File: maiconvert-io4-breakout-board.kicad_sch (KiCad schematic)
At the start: 86 parts, among them J1 CN3 - From IO4, J10 1P B7, J11 1P B8, J12 2P B1, J13 2P B2, J14 2P B3, J15 2P B4, J16 2P B5, J17 2P B6, J18 2P B7, J19 2P B8, J2 CN9 - From IO4, J20 1P SELECT BUTTON, J21 2P SELECT BUTTON, J22 12V input, J23 BILLBOARD LED L, J24 BILLBOARD LED R, J25 1P CODE READER LED, J26 2P CODE READER LED, J27 COIN METER, J28 COIN LOCKOUT, J29 CAMERA LED RED, J3 CN3 - To Harness, J30 CAMERA LED WARM, J31 TEST BUTTON, J32 COIN BUTTON, J33 SERVICE BUTTON, J4 1P B1, J5 1P B2, J6 1P B3, J7 1P B4, J8 1P B5, J9 1P B6, SW1 TEST, SW10 1P B5 BTN, SW11 1P B6 BTN, SW12 1P B7 BTN, SW13 1P B8 BTN, SW14 2P B1 BTN, SW15 2P B2 BTN, SW16 2P B3 BTN, SW17 2P B4 BTN, SW18 2P B5 BTN, SW19 2P B6 BTN, SW2 COIN, SW20 2P B7 BTN, SW21 2P B8 BTN, SW3 SERVICE, SW4 1P SELECT BTN, SW5 2P SELECT BTN, SW6 1P B1 BTN, SW7 1P B2 BTN, SW8 1P B3 BTN, SW9 1P B4 BTN

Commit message: Refactor project and prepare for prerelease
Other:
- title: maiConvert IO4 hat -> maiConvert IO4 breakout board

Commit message: Review and polish
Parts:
- J3: value CN3 - To Harness -> CN3 - To Harness (Passthrough)
- renumbered D21 to D3, D22 to D4
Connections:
- net EXV: now reaches J3.1 (Pin_1)
- net EXV: now also J1.1 (Pin_1), J1.2 (Pin_2), J3.2 (Pin_2)
- net NC 17: now reaches J3.17 (Pin_17)
- net NC 17: now also J1.17 (Pin_17)
- net NC 18: now reaches J3.18 (Pin_18)
- net NC 18: now also J1.18 (Pin_18)
- net NC 23: now reaches J3.23 (Pin_23)
- net NC 23: now also J1.23 (Pin_23)
- net NC 24: now reaches J3.24 (Pin_24)
- net NC 24: now also J1.24 (Pin_24)
- net NC 25: now reaches J3.25 (Pin_25)
- net NC 25: now also J1.25 (Pin_25)
- net NC 28: now reaches J3.28 (Pin_28)
- net NC 28: now also J1.28 (Pin_28)
- net NC 42: now reaches J3.42 (Pin_42)
- net NC 42: now also J1.42 (Pin_42)
- net NC 44: now reaches J3.44 (Pin_44)
- net NC 44: now also J1.44 (Pin_44)
- net NC 46: now reaches J3.46 (Pin_46)
- net NC 46: now also J1.46 (Pin_46)
- net NC 47: now reaches J3.47 (Pin_47)
- net NC 47: now also J1.47 (Pin_47)
- net NC 48: now reaches J3.48 (Pin_48)
- net NC 48: now also J1.48 (Pin_48)
- net NC 50: now reaches J3.50 (Pin_50)
- net NC 50: now also J1.50 (Pin_50)
- net NC 54: now reaches J3.54 (Pin_54)
- net NC 54: now also J1.54 (Pin_54)
- no-connect marks 39 -> 9

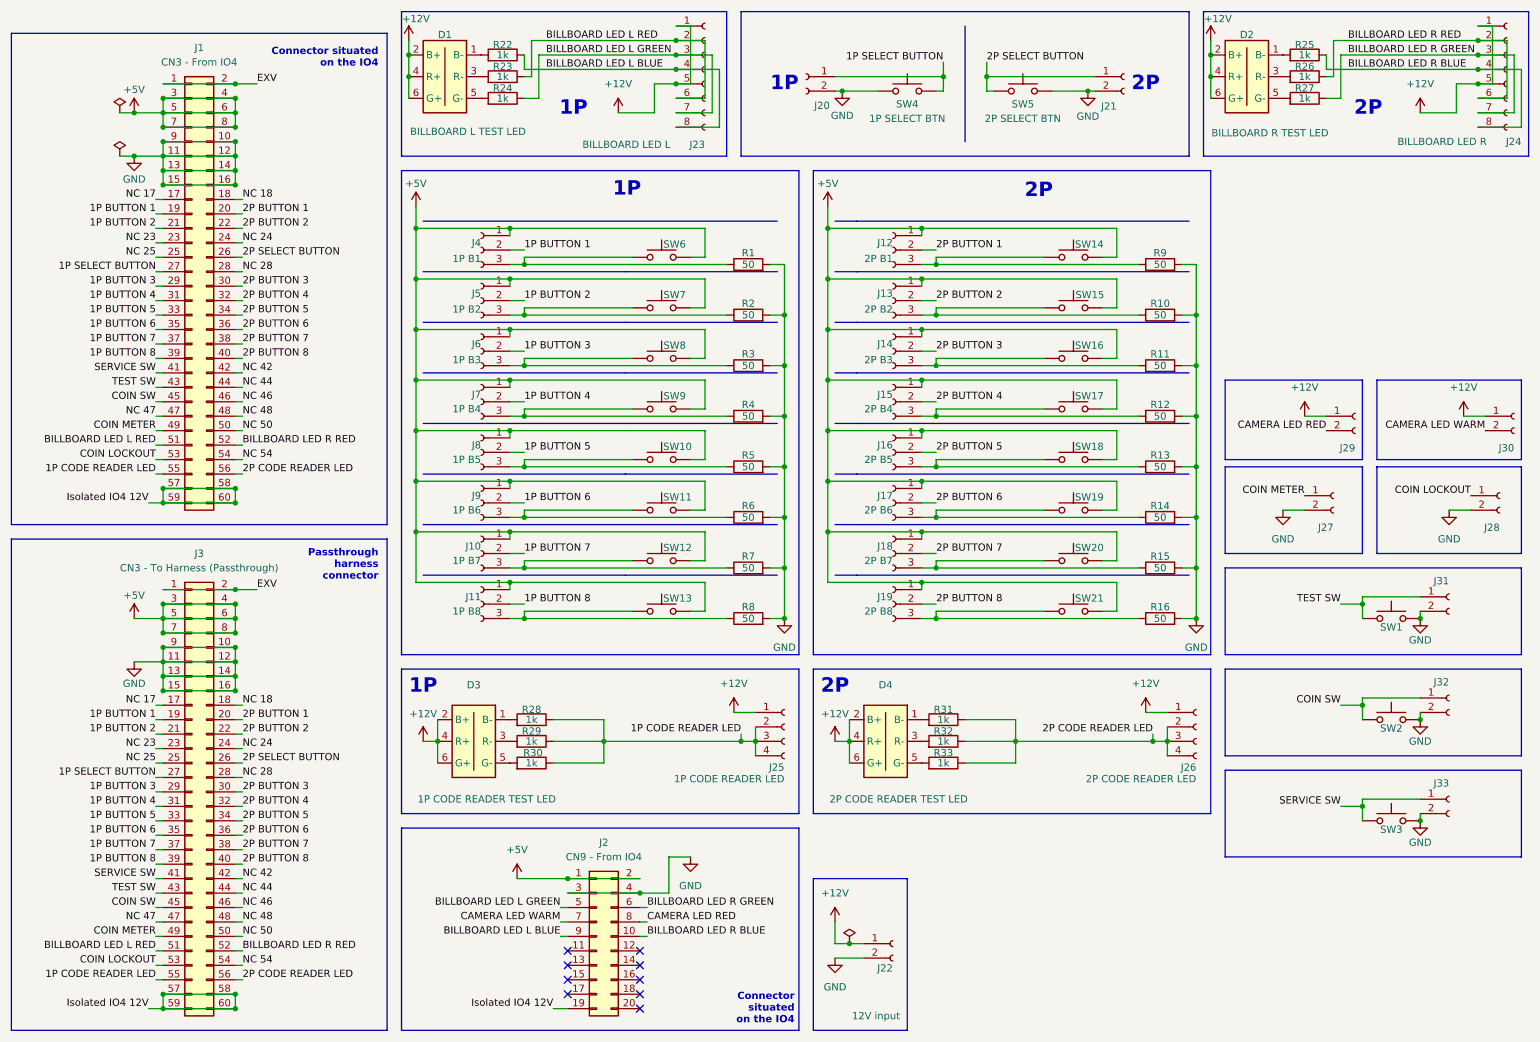
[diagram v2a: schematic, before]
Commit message: Add 12v input protaction
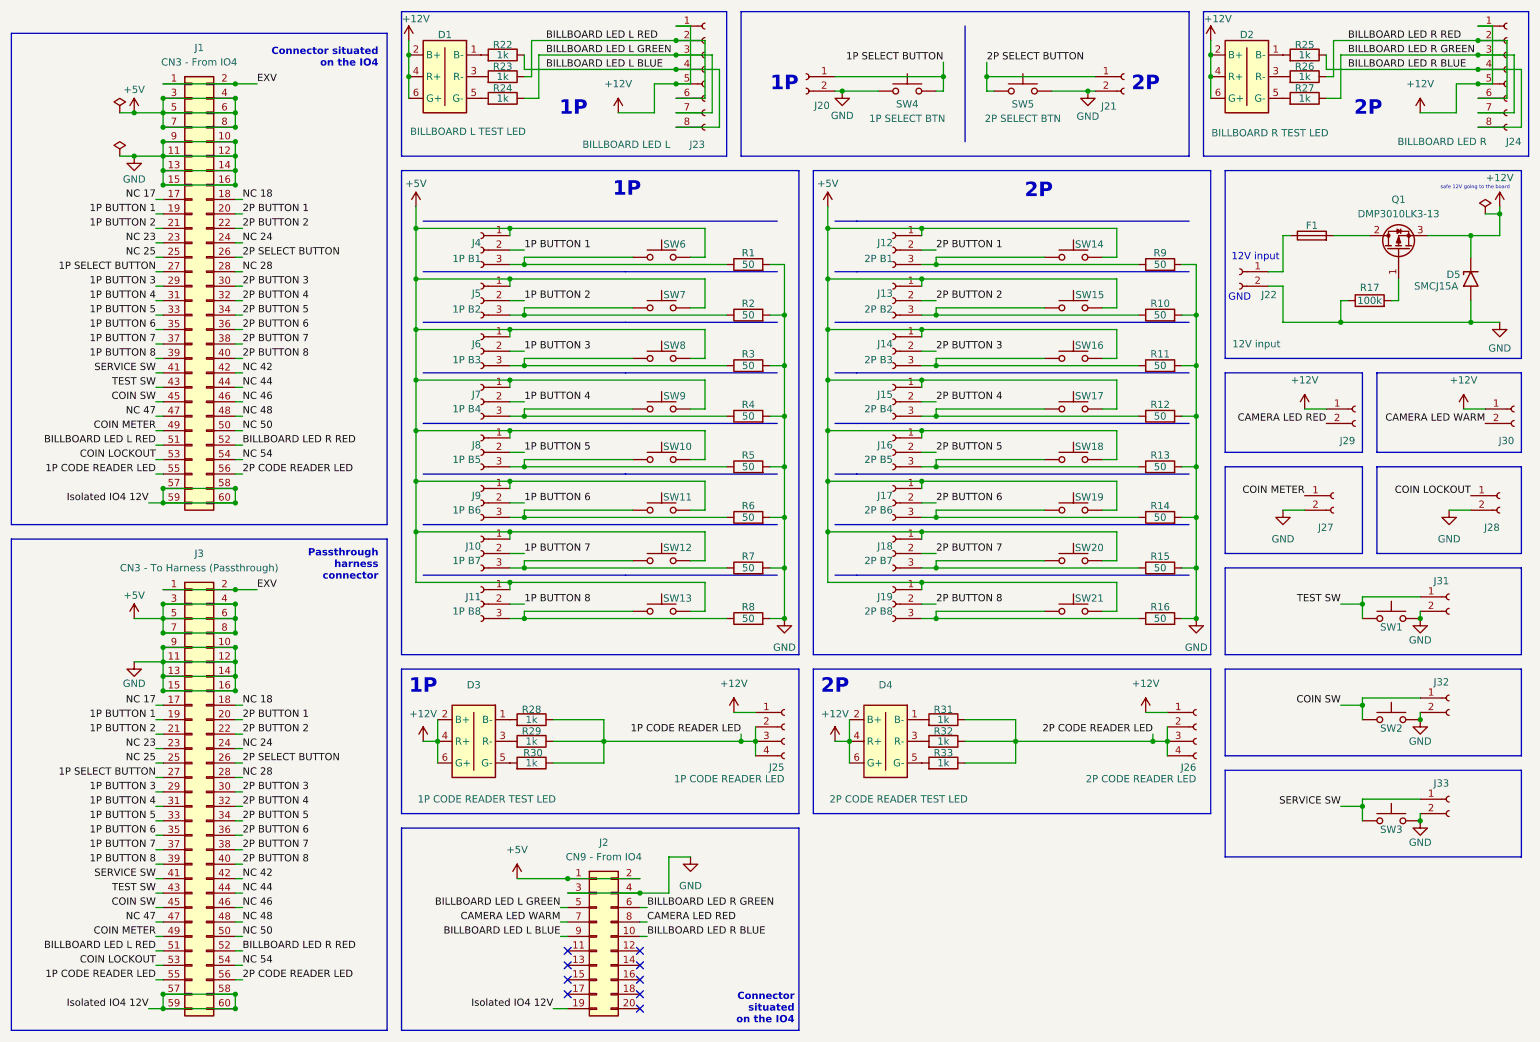
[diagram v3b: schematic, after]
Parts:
- added D5: SMCJ15A, Diode_SMD:D_SMC, symbol Diode:1.5SMCxxA
- added F1: 15A, Fuse:Fuse_Littelfuse-NANO2-451_453, symbol Device:Fuse
- added Q1: DMP3010LK3-13, Package_TO_SOT_SMD:TO-252-2, symbol Transistor_FET:Q_PMOS_GDS
- added R17: 100k, Resistor_SMD:R_0805_2012Metric_Pad1.20x1.40mm_HandSolder, symbol Device:R
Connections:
- net +12V: now also D5.1 (A1), Q1.3 (S); no longer J22.1 (Pin_1)
- net GND: now also D5.2 (A2), R17.1
- new net: F1.1, J22.1 (Pin_1)
- new net: F1.2, Q1.2 (D)
- new net: Q1.1 (G), R17.2
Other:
- note added: "12V input"
- note added: "GND"
- note added: "safe 12V going to the board"
- moved on the sheet: J22, J29, J30

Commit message: Update fuse reference
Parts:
- F1: Digi-Key F2593CT-ND -> 5923-0679L9150-05CT-ND; Manufacturer Littelfuse -> Bel Fuse; Mfr. No. 0451015.MRL -> 0679L9150-05
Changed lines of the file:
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@@
 			)
 		)
-		(property "Datasheet" "https://www.littelfuse.com/products/fuses-overcurrent-protection/fuses/surface-mount-fuses/nano-2-fuses/451/0451015"
+		(property "Datasheet" "https://belfuse.com/media/datasheets/products/circuit-protection/ds-cp-0679l-series.pdf"
 			(at 245.11 53.34 0)
 			(effects
@@
 			)
 		)
-		(property "Description" "Fuse 15A fast-acting, 65V, SMD Nano2 (Littelfuse 451). Overcurrent protection on the J22 12V input."
+		(property "Description" "Fuse 15A fast-acting, 125V, SMD Nano2/2410 (Bel Fuse 0679L, second-source for Littelfuse 451). Overcurrent protection on the J22 12V input."
 			(at 245.11 53.34 0)
 			(effects
@@
 			)
 		)
-		(property "Manufacturer" "Littelfuse"
+		(property "Manufacturer" "Bel Fuse"
 			(at 245.11 53.34 0)
 			(effects
@@
 			)
 		)
-		(property "Mfr. No." "0451015.MRL"
+		(property "Mfr. No." "0679L9150-05"
 			(at 245.11 53.34 0)
 			(effects
@@
 			)
 		)
-		(property "Digi-Key" "F2593CT-ND"
+		(property "Digi-Key" "5923-0679L9150-05CT-ND"
 			(at 245.11 53.34 0)
 			(effects

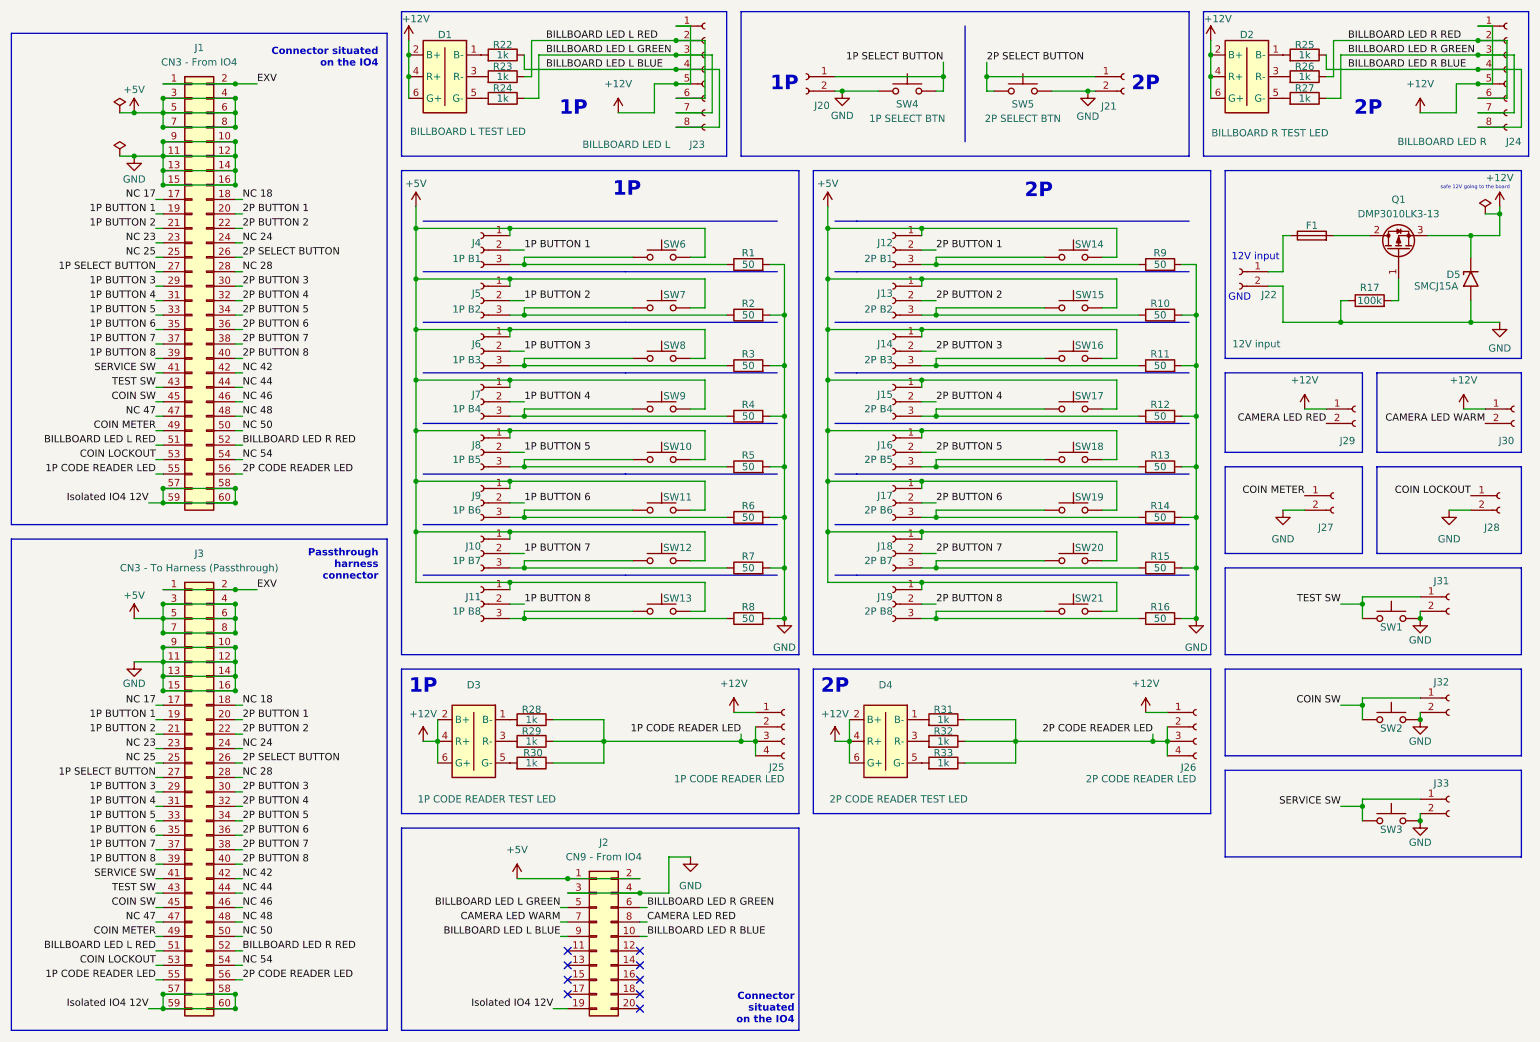
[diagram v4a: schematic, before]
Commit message: Add onboard bridge pins to allow user to specify harness structure
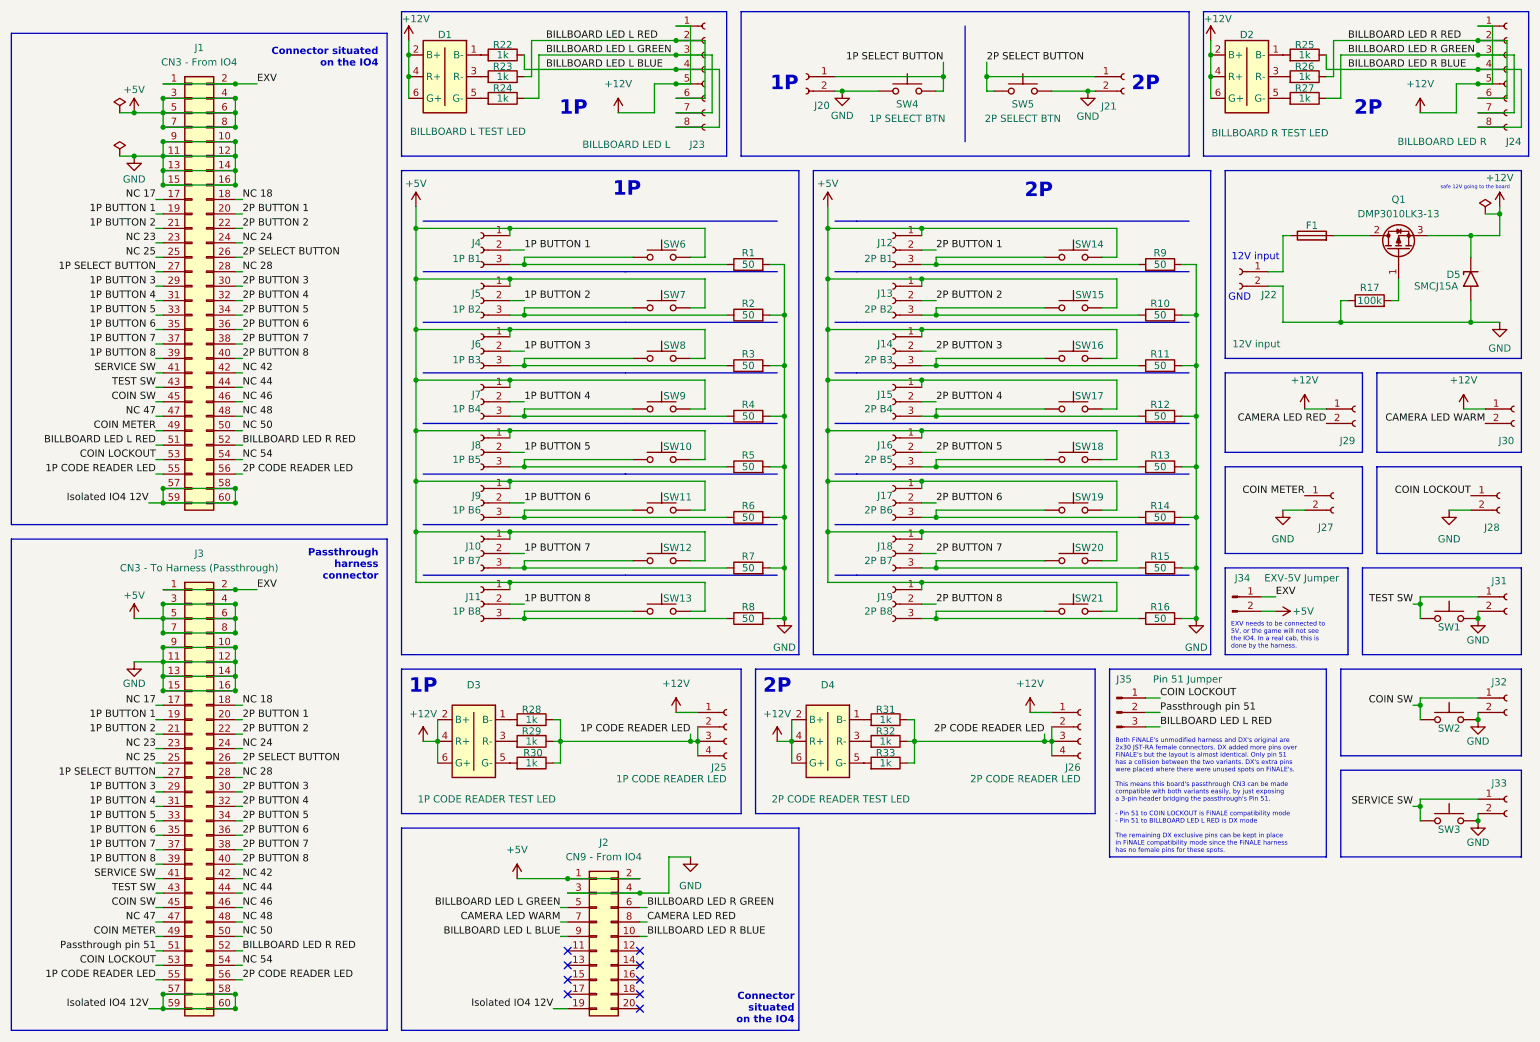
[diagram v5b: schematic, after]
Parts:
- added J34: EXV-5V Jumper, Connector_PinHeader_2.54mm:PinHeader_1x02_P2.54mm_Vertical, symbol Connector:Conn_01x02_Pin
- added J35: Pin 51 Jumper, Connector_PinHeader_2.54mm:PinHeader_1x03_P2.54mm_Vertical, symbol Connector:Conn_01x03_Pin
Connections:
- net +5V: now also J34.2 (Pin_2)
- net BILLBOARD LED L RED: now also J35.3 (Pin_3); no longer J3.51 (Pin_51)
- net COIN LOCKOUT: now also J35.1 (Pin_1)
- net EXV: now also J34.1 (Pin_1)
- new net Passthrough pin 51: J3.51 (Pin_51), J35.2 (Pin_2)
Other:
- note added: "Both FiNALE's unmodified harness and DX's original are 2x30 JST-RA female connectors. DX added more pins over FiNALE's but the layout is almost identical. Only pin 51 has a collision between the two variants. DX's extra pins were placed where there were unused spots on FiNALE's. This means this board's passthrough CN3 can be made compatible with both variants easily, by just exposing a 3-pin head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"
- note added: "EXV needs to be connected to 5V, or the game will not see the IO4. In a real cab, this is done by the harness."
- moved on the sheet: D4, J25, J26, J31, J32, J33, R31, R32, R33, SW1, SW2, SW3
